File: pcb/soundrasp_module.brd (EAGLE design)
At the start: 50 x 50 mm, 65 parts, among them IC1 74HC165D, IC2 ULN2003AD, SW1 EC12E_SW, SW2 EC12E_SW

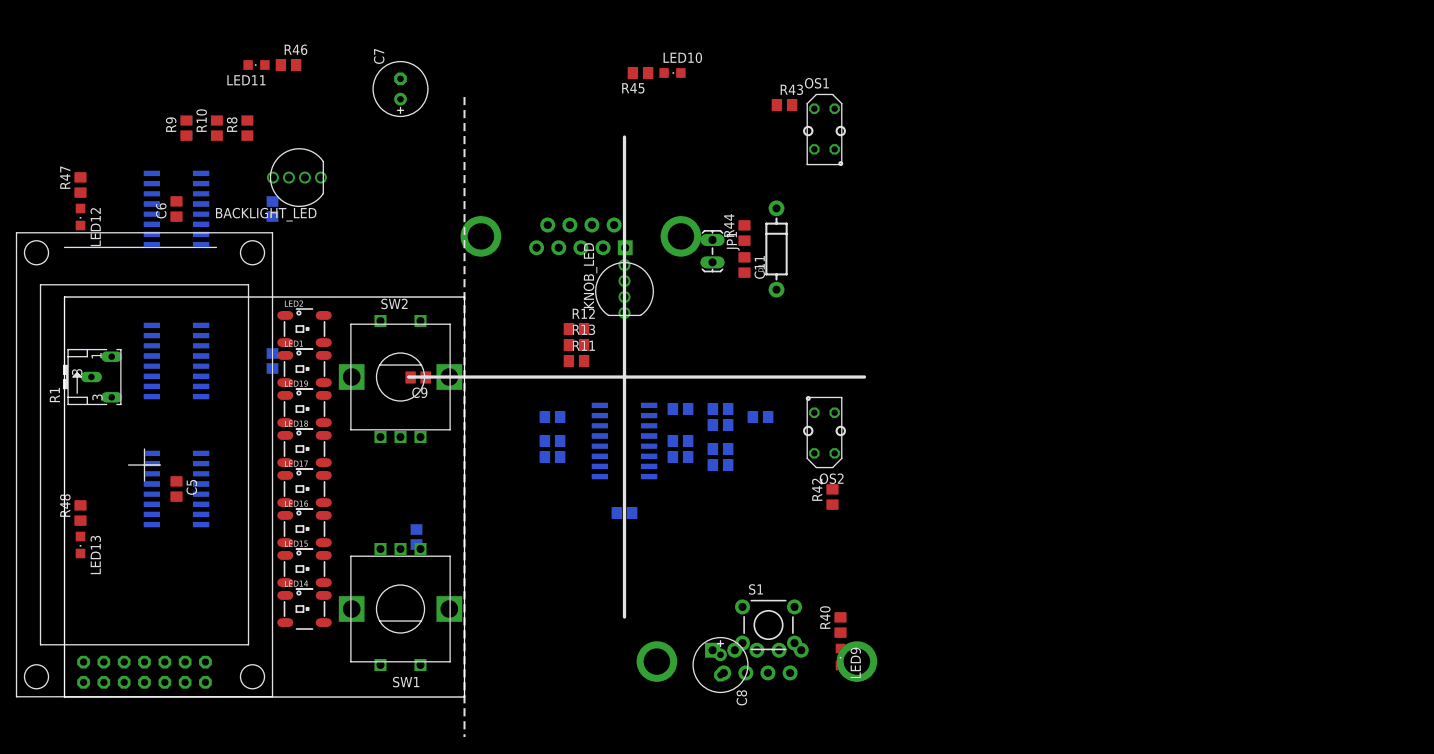
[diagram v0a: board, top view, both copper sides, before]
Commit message: Refactoring scema and doing initial pcb layout.
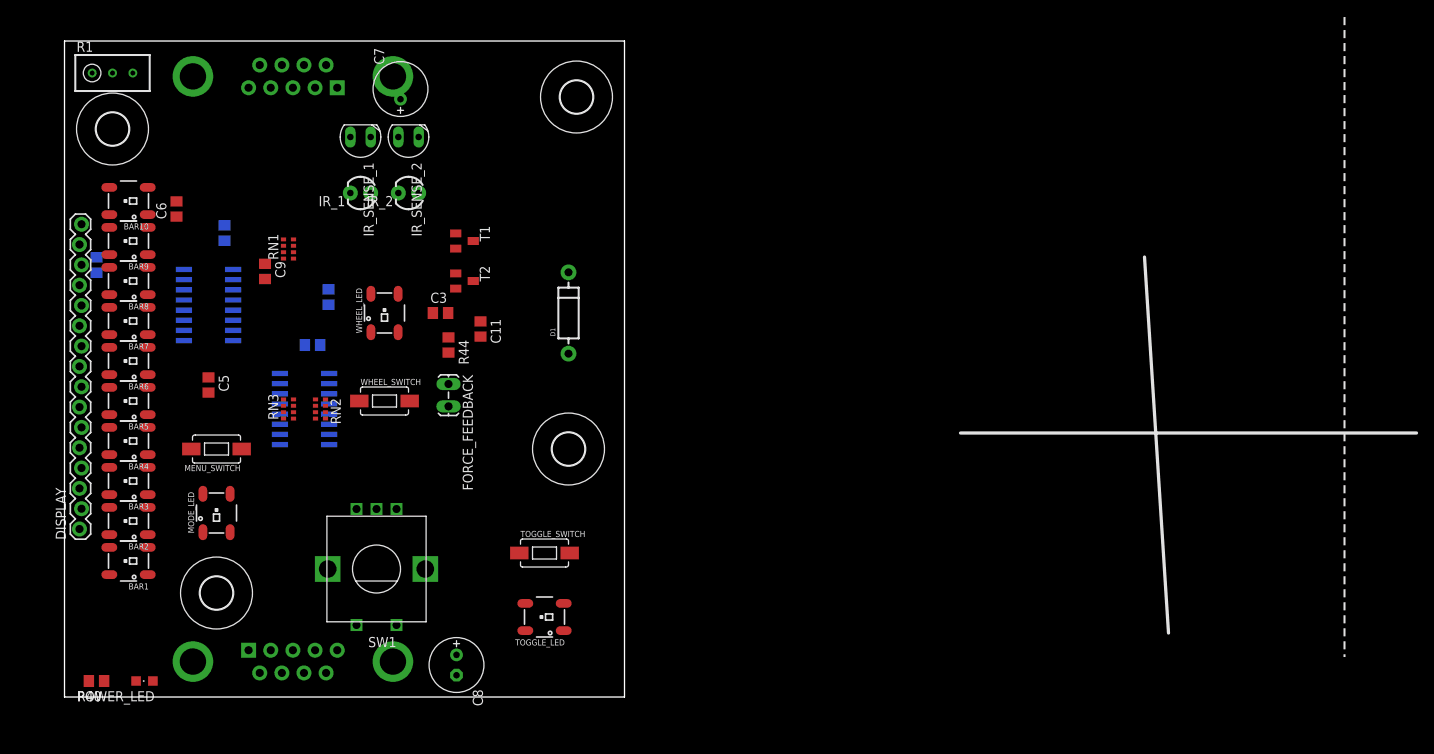
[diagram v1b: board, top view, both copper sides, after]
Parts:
- removed BACKLIGHT_LED, KNOB_LED: LED, SparkFun:LED-TRICOLOR-THROUGHHOLE
- removed C10, C12: 1uF, rcl:C0805
- removed IC2: ULN2003AD, uln-udn:SO16
- removed INDICATOR_SHIFT: 74HC595D, 74xx-eu:SO16
- removed JP1: (no value), SparkFun:1X02_LOCK_LONGPADS
- removed LED1, LED14, LED15, LED16, LED17, LED18, LED19, LED2: WS2812B, WS2812:WS2812B
- removed LED10, LED11, LED12, LED13, LED9: (no value), led:CHIPLED_0805
- removed OS1, OS2: (no value), tcrt5000:TCRT5000
- removed R10, R11, R12, R13, R8, R9: (no value), rcl:R0805
- removed R2, R3, R4, R5, R6, R7: 10k, rcl:R0805
- removed R38, R41: 100k, rcl:R0805
- removed R42, R43: 200 Ohm, rcl:R0805
- removed R45, R46, R47, R48: 220, rcl:R0805
- removed S1: (no value), SparkFun:TACTILE-PTH
- removed SW2: EC12E_SW, switch-alps:ALPS_EC12E_SW
- removed U$1: CHARACTER_LCD_8X2RT0802, character_lcd_RT0802B-1:RT0802B-1
- added BAR1, BAR10, BAR2, BAR3, BAR4, BAR5, BAR6, BAR7, BAR8, BAR9, MODE_LED, TOGGLE_LED, WHEEL_LED: WS2812B, WS2812:WS2812B
- added DISPLAY: M16LOCK, SparkFun-Connectors:1X16_LOCK
- added FORCE_FEEDBACK: (no value), SparkFun:1X02_LOCK_LONGPADS
- added H1, H2, H3, H4: MOUNT-HOLE4.1, holes:4,1
- added IR_1, IR_2: (no value), SparkFun-LED:LED3MM
- added IR_SENSE_1, IR_SENSE_2: SFH205, opto-trans-siemens:SFH205
- added MENU_SWITCH, TOGGLE_SWITCH, WHEEL_SWITCH: SWITCH-MOMENTARY-2-SMD-1101NE, SparkFun-Electromechanical:TACTILE-SWITCH-1101NE
- added POWER_LED: (no value), led:CHIPLED_0805
- added RN1: 220R, resistor-dil:0603-ARV
- added RN2, RN3: 10k, resistor-dil:0603-ARV
- added T1, T2: (no value), transistor:SOT23-BEC
- R1: device pot:B25X -> rcl:RTRIM3296W
- moved R40 93.3 mm to (4.00, 2.00), turned to 180 degrees
- moved X1 58.0 mm to (28.6, 4.43)
- moved R39 56.0 mm to (33.0, 50.0), turned to 90 degrees
- moved X2 41.2 mm to (28.6, 77.6)
- moved IC1 40.2 mm to (30.0, 36.0)
- moved R44 39.6 mm to (48.0, 44.0), turned to 270 degrees
- moved R1 38.1 mm to (6.00, 78.0), turned to 270 degrees
- moved C3 34.0 mm to (47.0, 48.0), flipped to the top
- moved C11 34.0 mm to (52.0, 46.0)
- moved C8 33.0 mm to (49.0, 4.00)
- moved C1 27.3 mm to (31.0, 44.0), turned to 0 degrees
- moved D1 27.2 mm to (63.0, 48.0)
- moved C4 25.1 mm to (4.00, 54.0)
- moved LCD_SHIFT 23.3 mm to (18.0, 49.0)
- moved C9 23.3 mm to (25.1, 53.2), turned to 270 degrees
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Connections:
- removed net N$14: BACKLIGHT_LED.RED, R8.2
- removed net N$18: KNOB_LED.BLU, R12.2
- removed net N$19: KNOB_LED.GRN, R13.2
- removed net N$24: INDICATOR_SHIFT.2, R10.1
- removed net N$25: INDICATOR_SHIFT.3, R11.1
- removed net N$29: LED1.4, LED19.2
- removed net N$74: OS2.A, R42.2
- removed net N$75: INDICATOR_SHIFT.14, LCD_SHIFT.9
- removed net N$76: INDICATOR_SHIFT.9
- removed net N$79: OS1.A, R43.2
- removed net N$81: INDICATOR_SHIFT.4, R12.1
- removed net N$82: INDICATOR_SHIFT.5, R13.1
- removed net N$83: IC2.1, INDICATOR_SHIFT.6
- removed net N$84: IC2.6, INDICATOR_SHIFT.7
- removed net N$85: IC2.2, IC2.3, LCD_SHIFT.6
- removed net N$88: IC2.4, IC2.5, LCD_SHIFT.7
- removed net N$89: IC2.15, LED10.C
- removed net N$90: LED10.A, R45.1
- removed net N$91: IC2.11, OS1.K, OS2.K
- removed net N$92: LED11.A, R46.1
- removed net N$93: IC2.14, LED11.C
- removed net N$94: LED12.A, R47.1
- removed net N$95: LED13.A, R48.1
- removed net N$96: IC2.13, LED12.C
- removed net N$97: IC2.12, LED13.C
- removed net V+: R45.2, R46.2, R47.2, R48.2
- new net BAR7: BAR6.2, BAR7.4
- new net CONTRAST: DISPLAY.3, R1.2
- new net D4: DISPLAY.11, LCD_SHIFT.1
- new net D5: DISPLAY.12, LCD_SHIFT.2
- new net D6: DISPLAY.13, LCD_SHIFT.3
- new net D7: DISPLAY.14, LCD_SHIFT.4
- new net E: DISPLAY.6, LCD_SHIFT.15
- new net LED_COLORS_IN: TOGGLE_LED.4, X1.5
- new net LED_COLORS_OUT: WHEEL_LED.2, X2.5
- new net R/W: DISPLAY.5
- new net RS: DISPLAY.4, LCD_SHIFT.5
- net +5V: now also BAR1.1, BAR10.1, BAR2.1, BAR3.1, BAR4.1, BAR5.1, BAR6.1, BAR7.1, BAR8.1, BAR9.1, DISPLAY.15, DISPLAY.2, FORCE_FEEDBACK.1, MODE_LED.1, R1.3, RN1.3, RN1.4, RN2.5, RN2.6, RN2.7, RN2.8, RN3.5, RN3.6, RN3.7, RN3.8, TOGGLE_LED.1, WHEEL_LED.1; no longer C10.1, C12.1, INDICATOR_SHIFT.10, INDICATOR_SHIFT.16, JP1.1, LED1.1, LED14.1, LED15.1, LED16.1, LED17.1, LED18.1, LED19.1, LED2.1, R1.E, R2.2, R3.2, R38.2, R4.2, R41.2, R42.1, R43.1, R5.2, R6.2, R7.2, U$1.P$2
- net GND: now also BAR1.3, BAR10.3, BAR2.3, BAR3.3, BAR4.3, BAR5.3, BAR6.3, BAR7.3, BAR8.3, BAR9.3, DISPLAY.1, DISPLAY.16, IR_SENSE_1.K, IR_SENSE_2.K, MENU_SWITCH.P$1, MODE_LED.3, POWER_LED.C, R1.1, T1.E, T2.E, TOGGLE_LED.3, TOGGLE_SWITCH.P$1, WHEEL_LED.3, WHEEL_SWITCH.P$1; no longer IC2.8, INDICATOR_SHIFT.13, INDICATOR_SHIFT.8, LED1.3, LED14.3, LED15.3, LED16.3, LED17.3, LED18.3, LED19.3, LED2.3, LED9.C, OS1.E, OS2.E, R1.A, S1.2, SW2.C, SW2.E, U$1.P$1, U$1.P$5
- net LED_VOLTAGE: no longer BACKLIGHT_LED.GND, KNOB_LED.GND, X1.5, X2.5
- net N$1: now also IR_1.A, RN1.6; no longer R1.S, U$1.P$3
- net N$10: now also BAR10.4, BAR9.2; no longer LCD_SHIFT.2, U$1.P$12
- net N$11: now also BAR10.2, WHEEL_LED.4; no longer LCD_SHIFT.3, U$1.P$13
- net N$12: now also MODE_LED.4, TOGGLE_LED.2; no longer LCD_SHIFT.4, U$1.P$14
- net N$13: now also BAR1.4, MODE_LED.2; no longer LCD_SHIFT.5, U$1.P$4
- net N$15: now also LCD_SHIFT.6, RN1.1; no longer BACKLIGHT_LED.BLU, R9.2
- net N$16: now also RN1.8, T1.B; no longer BACKLIGHT_LED.GRN, R10.2
- net N$17: now also LCD_SHIFT.7, RN1.2; no longer KNOB_LED.RED, R11.2
- net N$2: now also RN2.4; no longer R4.1
- net N$20: now also IR_1.K, IR_2.K, T2.C; no longer INDICATOR_SHIFT.15, R8.1
- net N$21: now also RN1.7, T2.B; no longer INDICATOR_SHIFT.1, R9.1
- net N$22: now also BAR1.2, BAR2.4; no longer LED14.2, LED15.4
- net N$23: now also BAR2.2, BAR3.4; no longer LED15.2, LED16.4
- net N$26: now also BAR3.2, BAR4.4; no longer LED16.2, LED17.4
- net N$27: now also BAR4.2, BAR5.4; no longer LED17.2, LED18.4
- net N$28: now also BAR5.2, BAR6.4; no longer LED18.2, LED19.4
- net N$3: now also RN2.3; no longer R5.1
- net N$30: now also BAR7.2, BAR8.4; no longer LED1.2, LED2.4
- net N$4: now also IR_SENSE_1.A, RN2.1; no longer R6.1, SW2.A
- net N$5: now also IR_SENSE_2.A, RN3.4; no longer R7.1, SW2.B
- net N$50: now also MENU_SWITCH.P$2, RN3.2; no longer C10.2, OS2.C, R41.1
- net N$6: now also RN2.2; no longer R2.1
- net N$7: now also RN3.3, WHEEL_SWITCH.P$2; no longer R3.1, S1.4, SW2.D
- net N$73: now also POWER_LED.A; no longer LED9.A
- net N$8: now also IR_2.A, RN1.5; no longer LCD_SHIFT.15, U$1.P$6
- net N$80: now also RN3.1, TOGGLE_SWITCH.P$2; no longer C12.2, OS1.C, R38.1
- net N$86: now also FORCE_FEEDBACK.2, T1.C; no longer IC2.16, JP1.2
- net N$9: now also BAR8.2, BAR9.4; no longer LCD_SHIFT.1, U$1.P$11
- net OUTPUT_CLOCK: no longer INDICATOR_SHIFT.11
- net OUTPUT_LATCH: no longer INDICATOR_SHIFT.12
- net OUTPUT_OUT: now also LCD_SHIFT.9
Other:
- board size 50 x 50 mm -> 70 x 82 mm

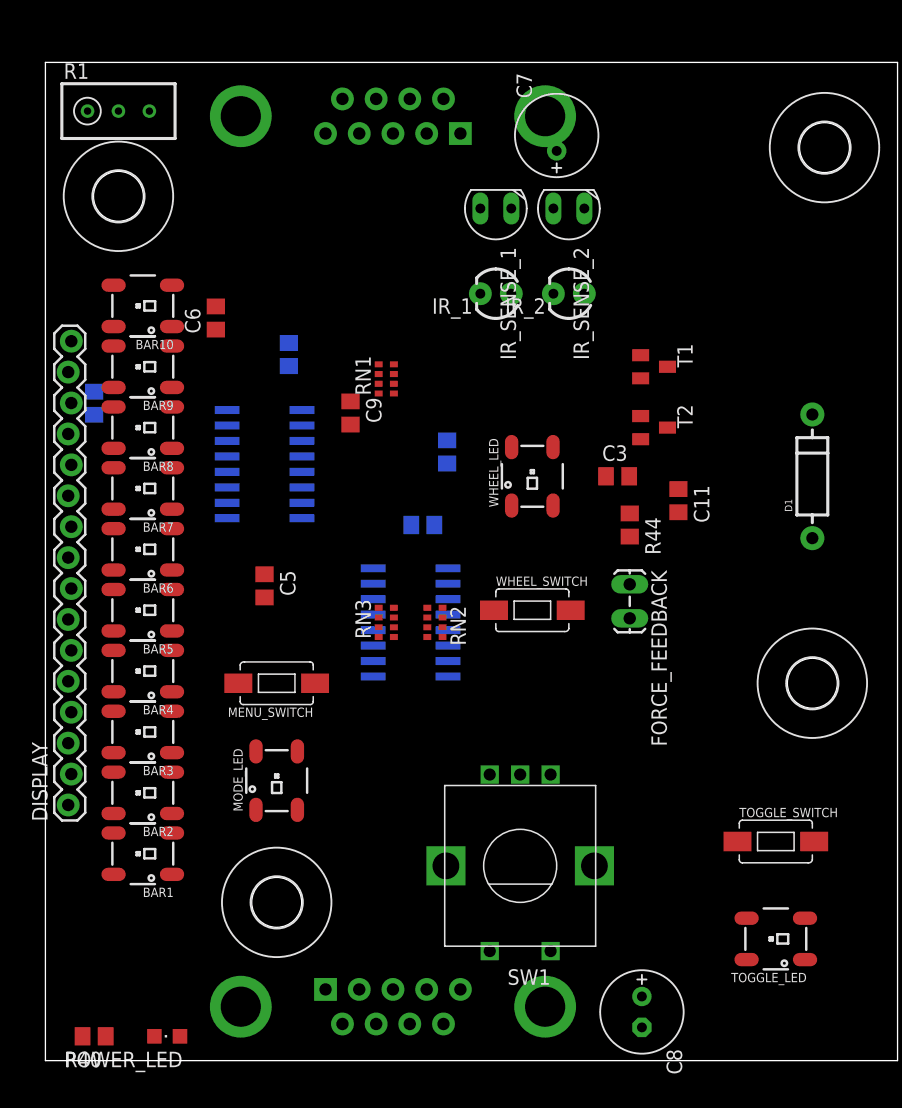
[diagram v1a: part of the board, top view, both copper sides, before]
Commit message: Removed force feedback. Changed design to use one common IR LED.
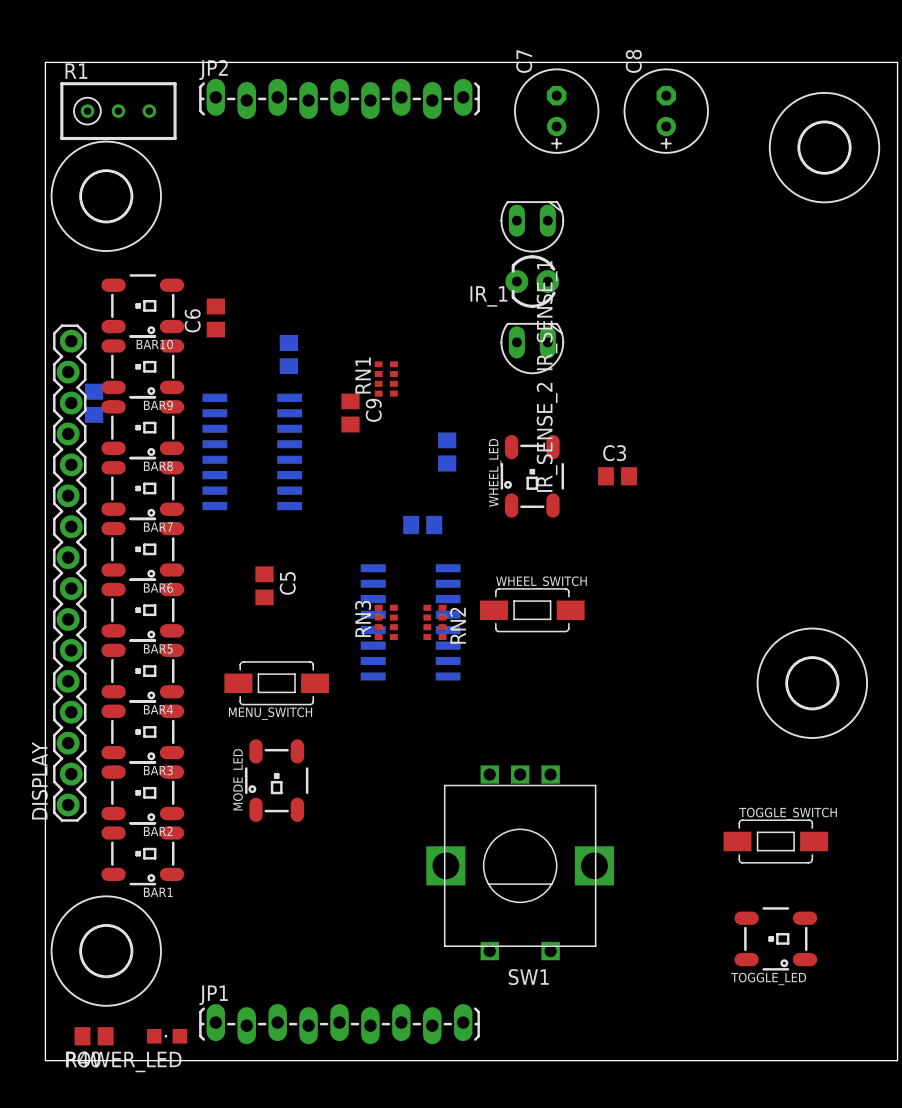
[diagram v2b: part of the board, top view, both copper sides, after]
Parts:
- removed C11: 1nF, rcl:C0805
- removed D1: (no value), SparkFun:DIODE-1N4001
- removed FORCE_FEEDBACK: (no value), SparkFun:1X02_LOCK_LONGPADS
- removed IR_2: (no value), SparkFun-LED:LED3MM
- removed R44: 100 Ohm, rcl:R0805
- removed T1, T2: (no value), transistor:SOT23-BEC
- removed X1: (no value), SparkFun:DB9_MALE
- removed X2: (no value), SparkFun:DB9
- added JP1, JP2: M09LOCK-LONGPADS, SparkFun:1X09_LOCK_LONGPADS
- moved C8 74.0 mm to (51.0, 78.0), turned to 90 degrees
- moved H4 14.6 mm to (5.00, 9.00)
- moved IR_SENSE_2 11.4 mm to (40.0, 59.0)
- moved IR_1 3.16 mm to (40.0, 64.0)
- moved IR_SENSE_1 3.16 mm to (40.0, 69.0)
- moved C7 2.00 mm to (42.0, 78.0)
- moved LCD_SHIFT 1.41 mm to (17.0, 50.0)
- moved H1 1.00 mm to (5.00, 71.0)
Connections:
- removed net N$16: RN1.8, T1.B
- removed net N$17: LCD_SHIFT.7, RN1.2
- removed net N$20: IR_1.K, IR_2.K, T2.C
- removed net N$21: RN1.7, T2.B
- removed net N$8: IR_2.A, RN1.5
- removed net N$86: C11.2, D1.A, FORCE_FEEDBACK.2, T1.C
- removed net N$87: C11.1, R44.1
- net +5V: now also JP1.9, JP2.9; no longer D1.C, FORCE_FEEDBACK.1, R44.2, RN1.4, X1.9, X2.9
- net GND: now also JP1.1, JP2.1; no longer T1.E, T2.E, X1.1, X2.1
- net INPUT_CLOCK: now also JP1.7, JP2.7; no longer X1.7, X2.7
- net INPUT_IN: now also JP2.6; no longer X2.6
- net INPUT_LATCH: now also JP1.8, JP2.8; no longer X1.8, X2.8
- net INPUT_OUT: now also JP1.6; no longer X1.6
- net LED_COLORS_IN: now also JP1.5; no longer X1.5
- net LED_COLORS_OUT: now also JP2.5; no longer X2.5
- net N$15: now also IR_1.K; no longer RN1.1
- net OUTPUT_CLOCK: now also JP1.3, JP2.3; no longer X1.3, X2.3
- net OUTPUT_IN: now also JP1.2; no longer X1.2
- net OUTPUT_LATCH: now also JP1.4, JP2.4; no longer X1.4, X2.4
- net OUTPUT_OUT: now also JP2.2; no longer X2.2

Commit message: Tuned schema and board.
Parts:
- removed C4, C5, C6, C9: 100nF, rcl:C0805
- removed RN1: 220R, resistor-dil:0603-ARV
- added R2: 220R, rcl:R0805
- moved R40 39.0 mm to (43.0, 3.00)
- moved POWER_LED 38.0 mm to (48.0, 3.00), turned to 270 degrees
- moved C3 29.8 mm to (40.0, 77.0), turned to 270 degrees
- moved H2 24.0 mm to (63.0, 7.00)
- moved C1 16.6 mm to (24.0, 29.0), flipped to the top
- moved C2 14.0 mm to (19.0, 44.0), flipped to the top, turned to 180 degrees
- moved R1 13.0 mm to (17.0, 71.0)
- moved RN3 10.0 mm to (18.0, 37.0)
- moved R39 8.25 mm to (31.0, 42.0), flipped to the top, turned to 0 degrees
- moved MENU_SWITCH 8.06 mm to (20.0, 23.0)
- moved TOGGLE_LED 7.28 mm to (58.0, 17.0), turned to 90 degrees
- moved MODE_LED 7.07 mm to (20.0, 16.0)
- moved IC1 6.08 mm to (24.0, 37.0)
- moved TOGGLE_SWITCH 5.39 mm to (58.0, 23.0), turned to 180 degrees
- moved H1 4.47 mm to (7.00, 75.0)
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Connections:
- removed net LED_VOLTAGE: C7.+, C8.+, C9.1
- net +5V: now also C7.+, C8.+, R2.2; no longer C4.1, C5.1, C6.1, RN1.3
- net GND: no longer C4.2, C5.2, C6.2, C9.2
- net N$1: now also R2.1; no longer RN1.6

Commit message: Made LCD backlight controllable.
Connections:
- new net N$8: DISPLAY.16, LCD_SHIFT.7
- net GND: no longer DISPLAY.16
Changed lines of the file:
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@@
 <contactref element="WHEEL_SWITCH" pad="P$1"/>
 <contactref element="MENU_SWITCH" pad="P$1"/>
-<contactref element="DISPLAY" pad="16"/>
 <contactref element="TOGGLE_LED" pad="3"/>
 <contactref element="TOGGLE_SWITCH" pad="P$1"/>
@@
 <wire x1="39" y1="23.5" x2="36.85" y2="33" width="0" layer="19" extent="1-1"/>
 <wire x1="5.6" y1="59.7" x2="15.9266" y2="57.445" width="0" layer="19" extent="1-16"/>
-<wire x1="2.127" y1="59.1" x2="5.6" y2="59.7" width="0" layer="19" extent="1-1"/>
 <wire x1="5.6" y1="64.7" x2="5.6" y2="59.7" width="0" layer="19" extent="1-1"/>
 <wire x1="5.6" y1="54.7" x2="5.6" y2="59.7" width="0" layer="19" extent="1-1"/>
@@
 <wire x1="5.6" y1="16.3" x2="21.7" y2="13.6" width="0" layer="19" extent="1-1"/>
 </signal>
+<signal name="N$8">
+<contactref element="DISPLAY" pad="16"/>
+<contactref element="LCD_SHIFT" pad="7"/>
+<wire x1="2.127" y1="59.1" x2="15.9266" y2="56.175" width="0" layer="19" extent="16-16"/>
+</signal>
 </signals>
